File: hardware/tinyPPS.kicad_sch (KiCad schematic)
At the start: 64 parts, among them IC1 AP2205-33Y-13, IC2 AP33772SDKZ-13-FA01, J1 USB_C_Receptacle_USB2.0_14P, J2 187-3802, J3 187-3802, J5 SM03B-SRSS-TB_LF__SN_, Q1 DMN3009SFG-7, Q2 DMN3009SFG-7, Q3 BSS123, Q4 BSS123, SW1 RotaryEncoder_Switch, SW2 BOOT, U1 RP2040, U2 W25Q128JVEIM, U3 DM-OLED096-636, U4 INA226, Y1 ABM8-272-T3

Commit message: Change PCB size to 60x40mm and update INA226 circuit
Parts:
- added C25: 100n, Capacitor_SMD:C_0402_1005Metric, symbol Device:C
- added C4: 1u, Capacitor_SMD:C_0402_1005Metric, symbol Device:C
- added R19, R20: 10R, Resistor_SMD:R_0402_1005Metric, symbol Device:R
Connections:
- net GND: now also C4.2
- net PD_INT: now also U1.37 (GPIO25); no longer U1.28 (GPIO17)
- net VBUS: now also C4.1
- net VIN+: now also R19.1; no longer U4.10 (Vin+)
- net VBUS_PD renamed VOUT_PD
- net VOUT_PD: now also R20.1; no longer U4.8 (Vbus), U4.9 (Vin-)
- new net: C25.1, R19.2, U4.10 (Vin+)
- new net: C25.2, R20.2, U4.8 (Vbus), U4.9 (Vin-)
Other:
- note added: "6.4.2 Filtering and Input Considerations"
- moved on the sheet: C22, C23, R10, R9, U4

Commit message: Change footprint for flash to WSON-8 6x5mm and re-route the PCB
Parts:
- U2: footprint Package_SON:WSON-8-1EP_2x2mm_P0.5mm_EP0.9x1.6mm -> Package_SON:WSON-8-1EP_6x5mm_P1.27mm_EP3.4x4mm
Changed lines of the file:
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@@
 			)
 		)
-		(property "Footprint" "Package_SON:WSON-8-1EP_2x2mm_P0.5mm_EP0.9x1.6mm"
+		(property "Footprint" "Package_SON:WSON-8-1EP_6x5mm_P1.27mm_EP3.4x4mm"
 			(at 233.68 223.52 0)
 			(effects

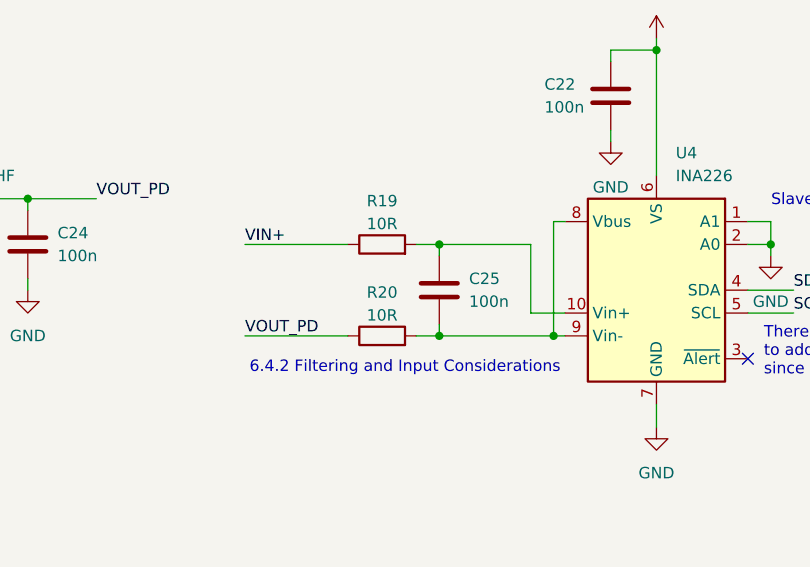
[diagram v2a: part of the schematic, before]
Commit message: Fix reading current from INA226
- Remove output filterfing from INA266, cause it may not be correctly
  implemented.
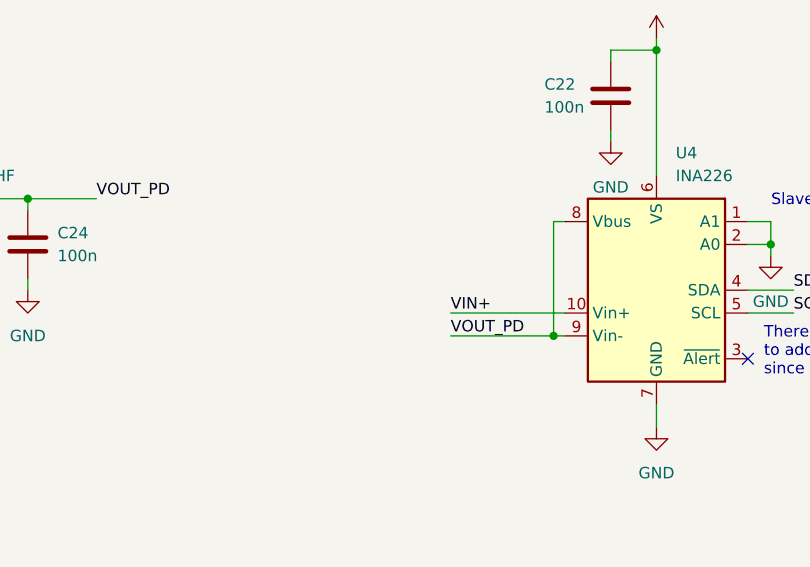
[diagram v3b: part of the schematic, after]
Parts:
- removed C25: 100n, Capacitor_SMD:C_0402_1005Metric, symbol Device:C
- removed R19, R20: 10R, Resistor_SMD:R_0402_1005Metric, symbol Device:R
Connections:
- net VIN+: now also U4.10 (Vin+)
- net VOUT_PD: now also U4.8 (Vbus), U4.9 (Vin-)
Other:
- note removed: "6.4.2 Filtering and Input Considerations"

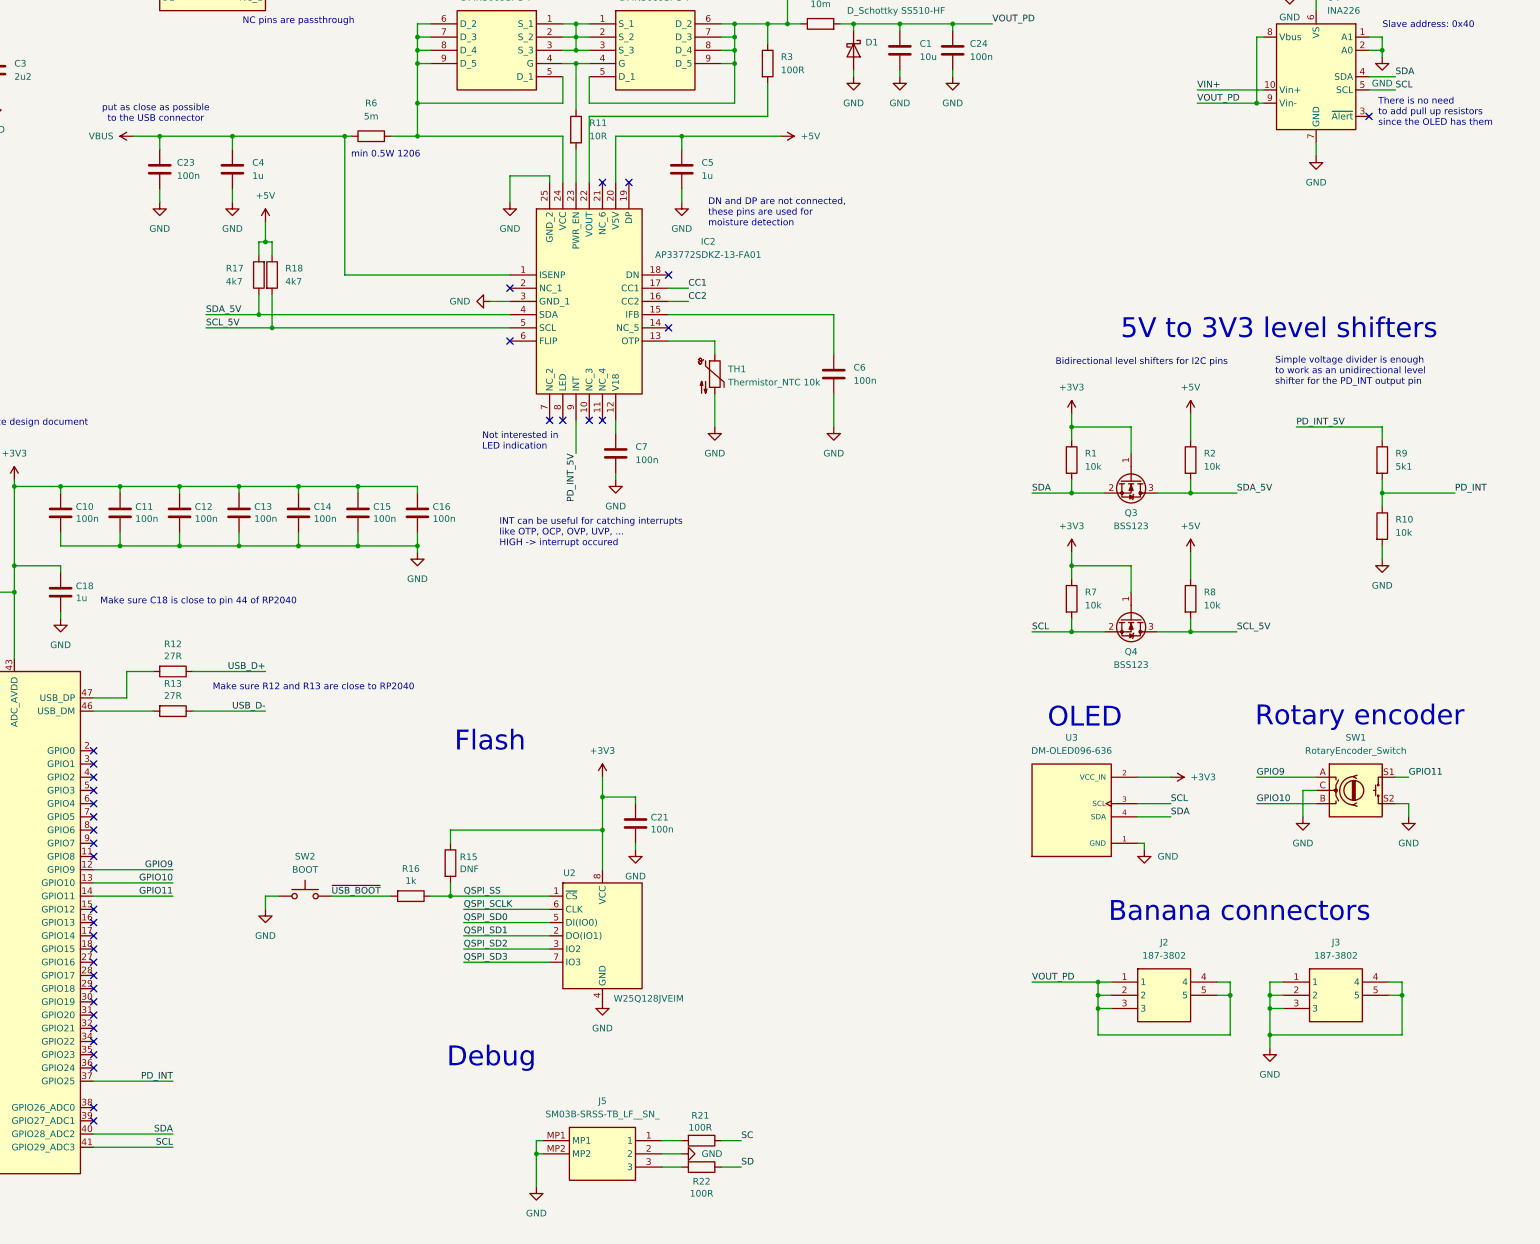
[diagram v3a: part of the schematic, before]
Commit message: Schematic: Remove i2c level shifters
AP33772s' i2c can operate at 3V3, there is no need for level shifters.
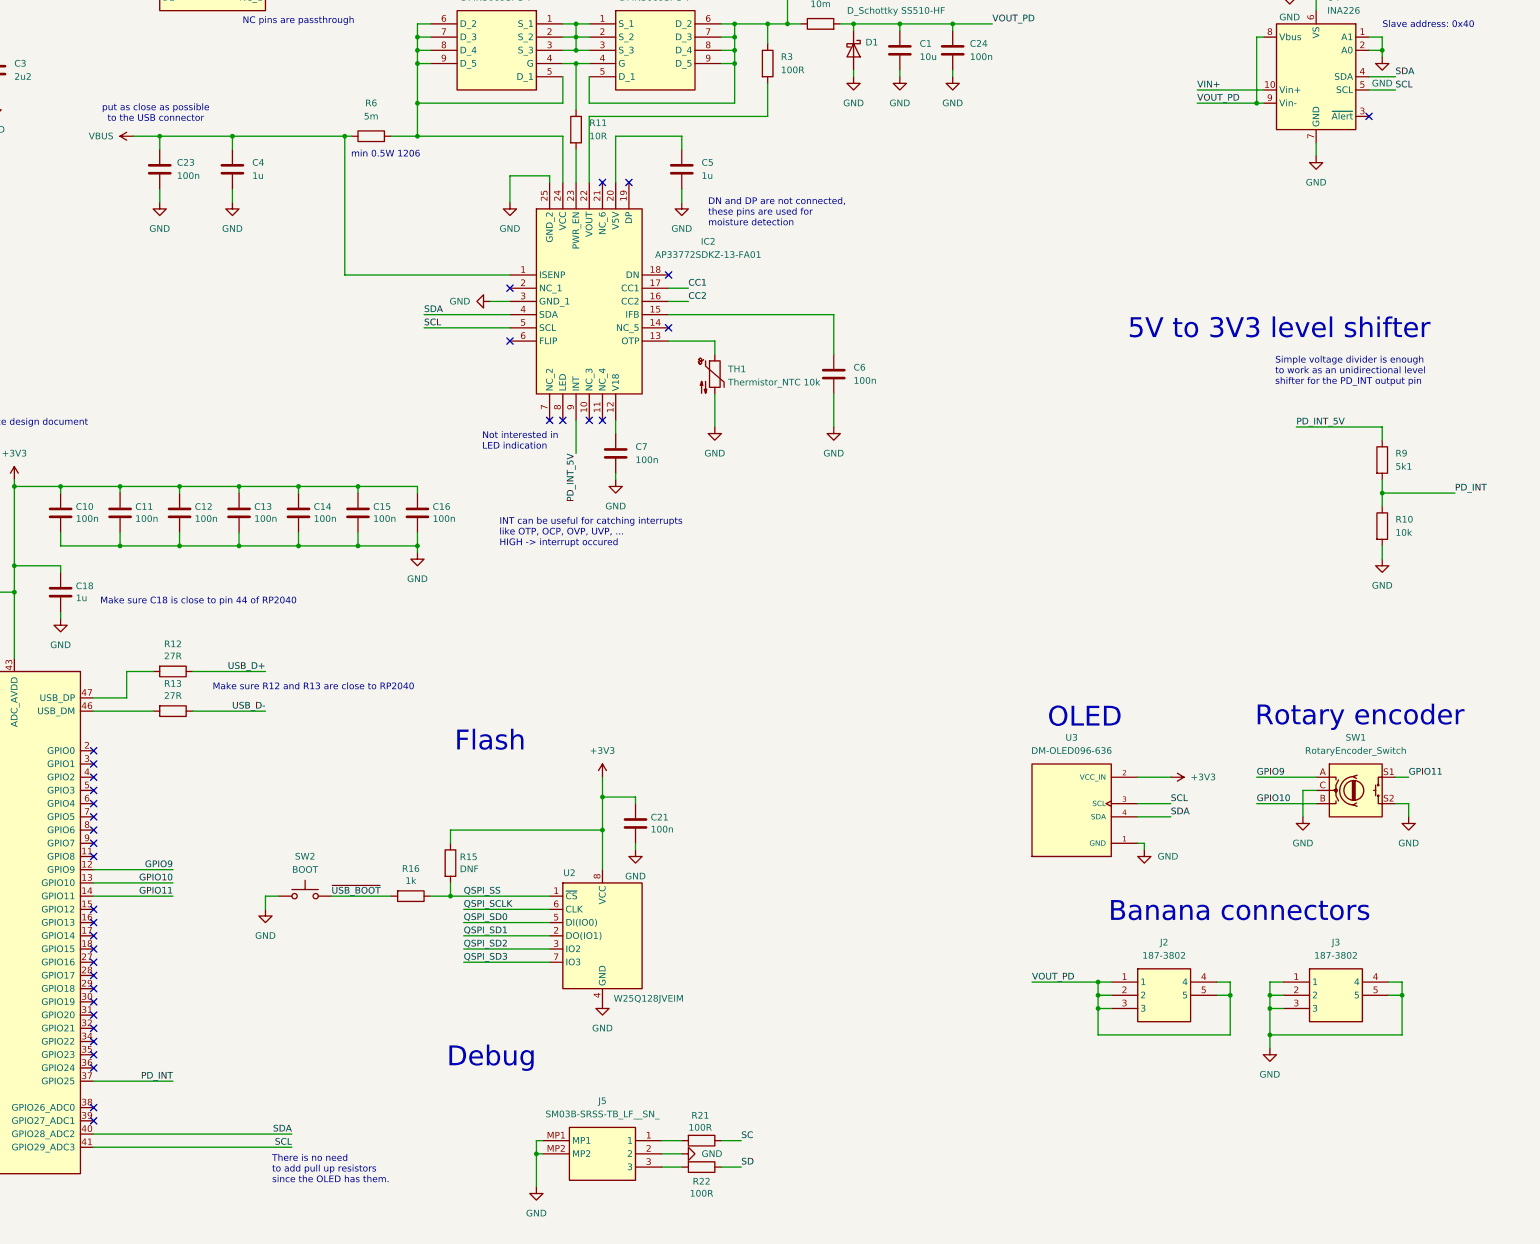
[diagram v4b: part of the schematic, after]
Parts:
- removed Q3, Q4: BSS123, Package_TO_SOT_SMD:SOT-23, symbol Transistor_FET:BSS123
- removed R1, R2, R7, R8: 10k, Resistor_SMD:R_0402_1005Metric, symbol Device:R
- removed R17, R18: 4k7, Resistor_SMD:R_0402_1005Metric, symbol Device:R
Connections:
- net SCL_5V is gone; now on net SCL: IC2.5 (SCL)
- net SDA_5V is gone; now on net SDA: IC2.4 (SDA)
- net +5V: no longer names the net of C5.1, IC2.20 (V5V)
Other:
- note added: "5V to 3V3 level shifter"
- note added: "There is no need to add pull up resistors since the OLED has them."
- note removed: "5V to 3V3 level shifters"
- note removed: "Bidirectional level shifters for I2C pins"
- note removed: "There is no need to add pull up resistors since the OLED has them"

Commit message: Hardware: Switch to 4-layer board setup
Schematic:
- Add TVS diodes to input and output
- Support both AP33772 and AP33772s
- Replace back-to-back NMOS swith with a single LM73100. AP33772(s) has a
  PWR_EN pin that is used as a gate driver for the NMOS switch. Voltage levels
  of the PWR_EN can be greater than the maximum rating of 6.5V for LM73100.
  Because of this, a Zener diode has been added to act as a voltage clamp.
- Since AP33772 has no capability to enable/disable the output (LM73100) via
  firmware (it is automatically enabled on successfull PD negotiation), a
  single 2-input AND gate (74LVC1G08GW,125) is added where one input is the
  PWR_EN signal from AP33772(s) and the other is RP2040's IO pin. The output is
  enabled only when the PD contract is negotiated and the vout_enable is set to
  true in firmware.
- Remove flyback protection
- Add test points for VOUT traces and the and gate inputs/output
- Add placeholders for I2C pull-up resistors.

PCB:
- Update physical stackup to match PCBWays setup
    - Thickness: 1.6mm
    - Finished Outer Copper: 1oz
    - Dielectric: 0.1960mm
    - Inner Copper: 1oz
    - Inner layer Residual copper ratio: 70%
- Setup netclass for USB with width and gap to match ~90ohm impedance
    - DP width: 0.24mm
    - DP gap: 0.15mm
    - Route PCB
- Change W25Q16JVUXIQ TR footprint to smaller 3x2mm package
- Update the 3D model of the PCB to represent the real PCB. 3D models of
  components have been updated with right models and colors.
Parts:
- removed D1: D_Schottky SS510-HF, Diode_SMD:D_SMA, symbol Device:D_Schottky
- removed Q1, Q2: DMN3009SFG-7, SamacSys:DMTH8008LFGQ7, symbol SamacSys:DMN3009SFG-7
- added C19, C24, C30: 100n, Capacitor_SMD:C_0402_1005Metric, symbol Device:C
- added C20: 100u/35v, Capacitor_SMD:CP_Elec_6.3x7.7, symbol Device:C_Polarized
- added C23: 1u, Capacitor_SMD:C_0805_2012Metric, symbol Device:C
- added C27: 22n, Capacitor_SMD:C_0402_1005Metric, symbol Device:C
- added D2, D4: TVS2200DRV, Package_SON:WSON-6-1EP_2x2mm_P0.65mm_EP1x1.6mm, symbol Power_Protection:TVS2200DRV
- added D3: 3v6, Diode_SMD:D_SOD-323, symbol Device:D_Zener
- added IC2: 74LVC1G08GW,125, 74LVC1G08GW,125:SOT65P210X110-5N, symbol 74LVC1G08GW,125:74LVC1G08GW,125
- added R16: 100k, Resistor_SMD:R_0402_1005Metric, symbol Device:R
- added R4: 1k, Resistor_SMD:R_0402_1005Metric, symbol Device:R
- added R7, R8: 4k7, Resistor_SMD:R_0402_1005Metric, symbol Device:R
- added TP1, TP2, TP3, TP4, TP5, TP6, TP7: TestPoint, TestPoint:TestPoint_Pad_D1.0mm, symbol Connector:TestPoint
- added U3: LM73100RPWR, LM73100RPWR:IC_LM73100RPWR, symbol LM73100RPWR:LM73100RPWR
- C22: value 100n -> 10u; footprint Capacitor_SMD:C_0402_1005Metric -> Capacitor_SMD:C_0805_2012Metric
- C28: renamed from C1; footprint Capacitor_SMD:C_1206_3216Metric -> Capacitor_SMD:C_0805_2012Metric
- J2: renamed from J5; footprint SM03BSRSSTBLFSN -> SamacSys:SM03BSRSSTBLFSN
- J4: renamed from J2; footprint 1873802 -> SamacSys:1873802
- J5: renamed from J3; footprint 1873802 -> SamacSys:1873802
- R10: renamed from R11; value 10R -> 10k
- R13: renamed from R15; now not fitted
- U2: value W25Q128JVEIM -> W25Q16JVUXIQ TR; footprint Package_SON:WSON-8-1EP_6x5mm_P1.27mm_EP3.4x4mm -> Package_SON:Winbond_USON-8-1EP_3x2mm_P0.5mm_EP0.2x1.6mm
- U4: value INA226 -> INA226AIDGSR; footprint Package_SO:VSSOP-10_3x3mm_P0.5mm -> Package_SO:TSSOP-10_3x3mm_P0.5mm
- renumbered C19 to C1, C12 to C10, C13 to C11, C4 to C12, C14 to C13, C15 to C14, C16 to C15, C7 to C16, C5 to C17, C6 to C18, C20 to C2, C2 to C25, C3 to C26, C24 to C29, C8 to C3, C9 to C4, C17 to C5, C23 to C6, C10 to C7, C18 to C8, C11 to C9, D2 to D1, IC2 to IC1, IC1 to IC3, U3 to J3, R4 to R1, R16 to R11, R3 to R12, R21 to R14, R22 to R15, R24 to R17, R9 to R18, R10 to R19, R5 to R2, R14 to R3, R12 to R5, R13 to R6, R6 to R9, SW2 to SW1, SW1 to SW2
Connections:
- net +3V3: now also C19.1, C30.1, IC2.5 (VCC), R7.1, R8.1, TP2.1; no longer C22.1
- net GND: now also J1.SH (SHIELD), C19.2, C20.2, C23.2, C24.2, C27.2, C30.2, D2.1 (GND), D2.2 (GND), D2.3 (GND), D2.7 (GND), D3.2 (A), D4.1 (GND), D4.2 (GND), D4.3 (GND), D4.7 (GND), IC2.3 (GND), R16.1, U3.2 (OVLO), U3.8 (GND), U3.9 (IMON); no longer J1.S1 (SHIELD)
- net SCL: now also U1.30 (GPIO19), R8.2; no longer U1.41 (GPIO29_ADC3)
- net SDA: now also U1.29 (GPIO18), R7.2; no longer U1.40 (GPIO28_ADC2)
- net VBUS: now also D2.4 (IN), D2.5 (IN), D2.6 (IN), TP1.1
- net VOUT_PD: now also C22.1, IC1.24 (VCC), R12.2, R9.2, C20.1, C23.1, C24.1, TP3.1, U3.5 (IN); no longer C28.1, C29.1, J4.1, J4.2, J4.3, J4.4, J4.5, R17.2, U4.8 (Vbus), U4.9 (Vin-)
- net D+: now reaches R5.2, U1.47 (USB_DP)
- net D-: now reaches R6.2, U1.46 (USB_DM)
- net PD_EN: now reaches R10.1
- net PD_EN: now also D3.1 (K), IC2.2 (A), TP5.1
- net at IC1.22 (VOUT): now also R12.1; no longer R12.2
- net at U1.17 (GPIO14): now also R4.2
- net MCU_EN: now reaches U1.28 (GPIO17)
- net MCU_EN: now also IC2.1 (B), TP6.1
- net VIN+ renamed VOUT_PD_SW
- net VOUT_PD_SW: now also TP7.1, U3.6 (OUT); no longer R12.1
- new net: C27.1, U3.7 (DVDT)
- new net VOUT: C28.1, C29.1, D4.4 (IN), D4.5 (IN), D4.6 (IN), J4.1, J4.2, J4.3, J4.4, J4.5, R17.2, U4.8 (Vbus), U4.9 (Vin-)
- new net VOUT_EN: IC2.4 (Y), R16.2, R4.1, TP4.1, U3.1 (EN/UVLO)
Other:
- note added: "100u cap acts as a buffer. It used to prevent the USB source from tripping its own OCP during transient events. Rest is just a HF filter."
- note added: "AP33772 and AP33772S are pin compatible"
- note added: "INPUT"
- note added: "Input ESD protection"
- note added: "MCU"
- note added: "Make sure C5 is close to pin 45 of RP2040"
- note added: "Make sure C8 is close to pin 44 of RP2040"
- note added: "Make sure R4 and R5 are close to RP2040"
- note added: "POWER SUPPLY CIRCUITRY"
- note added: "PWR_EN is a high-voltage gate driver and a zener diode is here to clamp the voltage to 3.6V"
- note added: "Place it near VOUT and LM73100"
- note added: "Put components as close as possible to the USB connector"
- note added: "TEST POINTS"
- note added: "USER INTERFACE"
- note added: "VOUT switch & short-circuit protection"
- note added: "VOUT_EN = MCU_EN & PD_EN VOUT is controlled by MCU, but it will be enabled only when there is no fault from AP33772(s)"
- note added: "put as close as possible to the VS pin"
- note removed: "Back-to-back N-MOS switch in common source configuration"
- note removed: "ESD protection"
- note removed: "Make sure C17 is close to pin 45 of RP2040"
- note removed: "Make sure C18 is close to pin 44 of RP2040"
- note removed: "Make sure R12 and R13 are close to RP2040"
- company: (none) -> Daniel Knezevic
- title: (none) -> Tiny Programmable Power Supply (tinyPPS)
- moved on the sheet: C1, C10, C11, C12, C13, C14, C15, C16, C17, C18, C2, C21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

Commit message: Hardware: Add a comment about how to choose the correct shunt
- AP33772 and AP33772S are using different shunts
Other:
- note added: "min 0.5W 1206 AP33772 uses 10m AP33772s uses 5m"
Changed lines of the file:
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@@
 		)
 	)
-	(text "min 0.5W 1206"
+	(text "min 0.5W 1206\nAP33772 uses 10m\nAP33772s uses 5m"
 		(exclude_from_sim no)
-		(at 212.852 106.172 0)
+		(at 213.106 108.458 0)
 		(effects
 			(font
